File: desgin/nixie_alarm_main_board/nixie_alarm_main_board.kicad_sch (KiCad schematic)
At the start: 1 part, among them U1 ESP32-S3-WROOM-1

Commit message: filter caps
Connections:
- net BUZZER: now also U1.6 (IO6); no longer U1.38 (IO2)
- net DEBUG_UART_RX: now also U1.36 (RXD0); no longer U1.25 (IO48)
- net DEBUG_UART_TX: now also U1.37 (TXD0); no longer U1.24 (IO47)
- net LED_DATA: now also U1.38 (IO2); no longer U1.6 (IO6)
- no-connect marks 11 -> 13

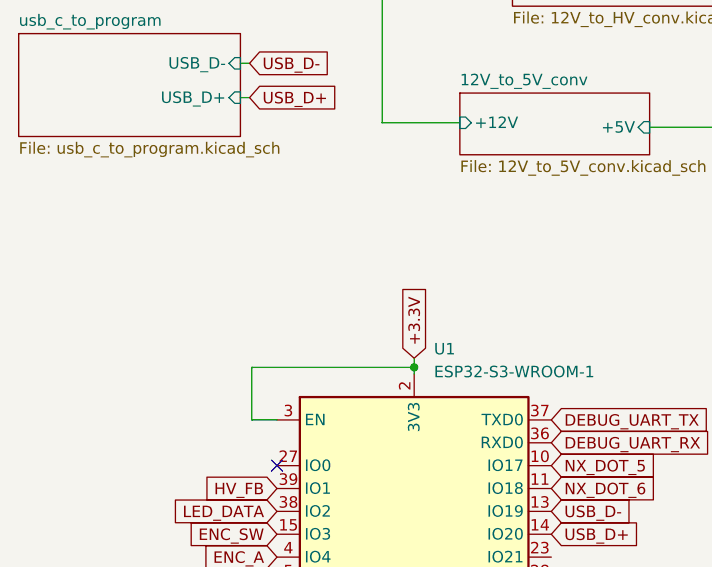
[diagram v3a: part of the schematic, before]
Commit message: all components in board footprint
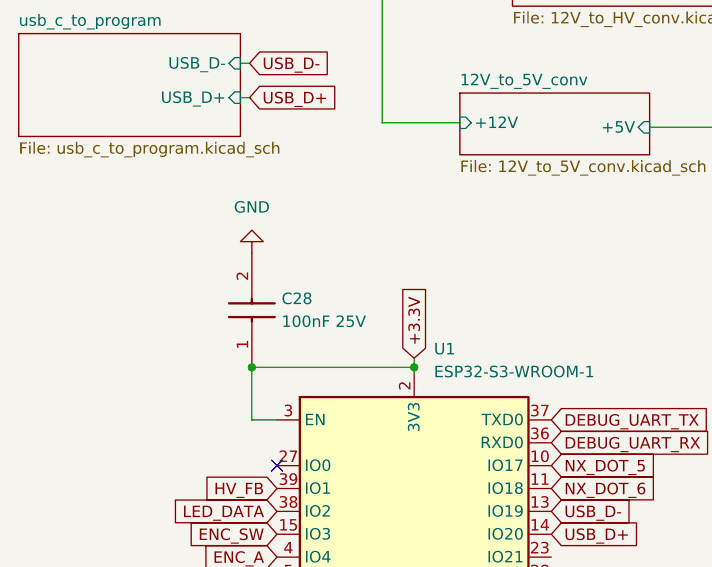
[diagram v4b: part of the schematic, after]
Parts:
- added C28: 100nF 25V, Capacitor_SMD:C_0805_2012Metric_Pad1.18x1.45mm_HandSolder, symbol SamacSys_Parts:GRM033R71E101KA01J
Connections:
- net +3.3V: now also C28.1
- net GND: now also C28.2
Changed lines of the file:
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@@
+		(color 0 0 0 0)
+	)
+	(junction
+		(at 109.474 81.28)
+		(diameter 0)
 		(color 0 0 0 0)
 	)
@@
 	)
 	(symbol
+		(lib_id "SamacSys_Parts:GRM033R71E101KA01J")
+		(at 109.474 81.28 90)
+		(unit 1)
+		(exclude_from_sim no)
+		(in_bom yes)
+		(on_board yes)
+		(dnp no)
+		(fields_autoplaced yes)
+		(property "Reference" "C28"
+			(at 112.776 73.6599 90)
+			(effects
+				(font
+					(size 1.27 1.27)
+				)
+				(justify right)
+			)
+		)
+		(property "Value" "100nF 25V"
+			(at 112.776 76.1999 90)
+			(effects
+				(font
+					(size 1.27 1.27)
+				)
+				(justify right)
+			)
+		)
+		(property "Footprint" "Capacitor_SMD:C_0805_2012Metric_Pad1.18x1.45mm_HandSolder"
+			(at 205.664 72.39 0)
+			(effects
+				(font
+					(size 1.27 1.27)
+				)
+				(justify left top)
+				(hide yes)
+			)
+		)
+		(property "Datasheet" "https://search.murata.co.jp/Ceramy/image/img/A01X/G101/ENG/GRM033R71E101KA01-01A.pdf"
+			(at 305.664 72.39 0)
+			(effects
+				(font
+					(size 1.27 1.27)
+				)
+				(justify left top)
+				(hide yes)
+			)
+		)
+		(property "Description" "Multilayer Ceramic Capacitors MLCC - SMD/SMT 100pF 25 volts 10%"
+			(at 109.474 81.28 0)
+			(effects
+				(font
+					(size 1.27 1.27)
+				)
+				(hide yes)
+			)
+		)
+		(property "Height" "0.5"
+			(at 505.664 72.39 0)
+			(effects
+				(font
+					(size 1.27 1.27)
+				)
+				(justify left top)
+				(hide yes)
+			)
+		)
+		(property "Mouser Part Number" "81-GRM033R71E101KA1J"
+			(at 605.664 72.39 0)
+			(effects
+				(font
+					(size 1.27 1.27)
+				)
+				(justify left top)
+				(hide yes)
+			)
+		)
+		(property "Mouser Price/Stock" "https://www.mouser.co.uk/ProductDetail/Murata-Electronics/GRM033R71E101KA01J?qs=563MOeNa05Lmru4oTW10Jw%3D%3D"
+			(at 705.664 72.39 0)
+			(effects
+				(font
+					(size 1.27 1.27)
+				)
+				(justify left top)
+				(hide yes)
+			)
+		)
+		(property "Manufacturer_Name" "Murata Electronics"
+			(at 805.664 72.39 0)
+			(effects
+				(font
+					(size 1.27 1.27)
+				)
+				(justify left top)
+				(hide yes)
+			)
+		)
+		(property "Manufacturer_Part_Number" "GRM033R71E101KA01J"
+			(at 905.664 72.39 0)
+			(effects
+				(font
+					(size 1.27 1.27)
+				)
+				(justify left top)
+				(hide yes)
+			)
+		)
+		(pin "1"
+		)
+		(pin "2"
+		)
+		(instances
+			(project "nixie_alarm_main_board"
+				(path "/a0d555d7-39a0-4a98-b831-70d97d0aa5a1"
+					(reference "C28")
+					(unit 1)
+				)
+			)
+		)
+	)
+	(symbol
 		(lib_id "power:GND")
 		(at 127.508 137.922 0)
@@
 					(unit 1)
 				)
+			)
+		)
+	)
+	(symbol
+		(lib_id "power:GND")
+		(at 109.474 68.58 180)
+		(unit 1)
+		(exclude_from_sim no)
+		(in_bom yes)
+		(on_board yes)
+		(dnp no)
+		(fields_autoplaced yes)
+		(property "Reference" "#PWR056"
+			(at 109.474 62.23 0)
+			(effects
+				(font
+					(size 1.27 1.27)
+				)
+				(hide yes)
+			)
+		)
+		(property "Value" "GND"
+			(at 109.474 63.5 0)
+			(effects
+				(font
+					(size 1.27 1.27)
+				)
+			)
+		)
+		(property "Footprint" ""
+			(at 109.474 68.58 0)
+			(effects
+				(font
+					(size 1.27 1.27)
+				)
+				(hide yes)
+			)
+		)
+		(property "Datasheet" ""
+			(at 109.474 68.58 0)
+			(effects
+				(font
+					(size 1.27 1.27)
+				)
+				(hide yes)
+			)
+		)
+		(property "Description" "Power symbol creates a global label with name \"GND\" , ground"
+			(at 109.474 68.58 0)
+			(effects
+				(font
+					(size 1.27 1.27)
+				)
+				(hide yes)
+			)
+		)
+		(pin "1"
+		)
+		(instances
+			(project "nixie_alarm_main_board"
+				(path "/a0d555d7-39a0-4a98-b831-70d97d0aa5a1"
+					(reference "#PWR056")
+					(unit 1)
+				)

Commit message: board v1
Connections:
- net BUZZER: now also U1.10 (IO17); no longer U1.6 (IO6)
- net DPOT_SCL: now also U1.24 (IO47); no longer U1.17 (IO9)
- net DPOT_SDA: now also U1.25 (IO48); no longer U1.12 (IO8)
- net ENC_A: now also U1.38 (IO2); no longer U1.4 (IO4)
- net ENC_B: now also U1.31 (IO38); no longer U1.5 (IO5)
- net ENC_SW: now also U1.21 (IO13); no longer U1.15 (IO3)
- net HV_FB: now also U1.11 (IO18); no longer U1.39 (IO1)
- net LED_DATA: now also U1.39 (IO1); no longer U1.38 (IO2)
- net NX_BL: now also U1.15 (IO3); no longer U1.18 (IO10)
- net NX_DATA_INPUT: now also U1.17 (IO9); no longer U1.7 (IO7)
- net NX_DOT_1: now also U1.4 (IO4); no longer U1.21 (IO13)
- net NX_DOT_2: now also U1.9 (IO16); no longer U1.22 (IO14)
- net NX_DOT_3: now also U1.12 (IO8); no longer U1.8 (IO15)
- net NX_DOT_4: now also U1.20 (IO12); no longer U1.9 (IO16)
- net NX_DOT_5: now also U1.22 (IO14); no longer U1.10 (IO17)
- net NX_DOT_6: now also U1.23 (IO21); no longer U1.11 (IO18)
- net NX_LE: now also U1.18 (IO10); no longer U1.20 (IO12)
- no-connect marks 13 -> 10

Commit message: new board v1
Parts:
- removed C28: 100nF 25V, Capacitor_SMD:C_0805_2012Metric_Pad1.18x1.45mm_HandSolder, symbol SamacSys_Parts:GRM033R71E101KA01J
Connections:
- net BUZZER: now also U1.22 (IO14); no longer U1.10 (IO17)
- net ENC_A: now also U1.39 (IO1); no longer U1.38 (IO2)
- net ENC_B: now also U1.38 (IO2); no longer U1.31 (IO38)
- net ENC_SW: now also U1.31 (IO38); no longer U1.21 (IO13)
- net LED_DATA: now also U1.4 (IO4); no longer U1.39 (IO1)
- net NX_BL: now also U1.19 (IO11); no longer U1.15 (IO3)
- net NX_CLK: now also U1.17 (IO9); no longer U1.19 (IO11)
- net NX_DATA_INPUT: now also U1.18 (IO10); no longer U1.17 (IO9)
- net NX_DOT_1: now also U1.5 (IO5); no longer U1.4 (IO4)
- net NX_DOT_2: now also U1.10 (IO17); no longer U1.9 (IO16)
- net NX_DOT_5: now also U1.21 (IO13); no longer U1.22 (IO14)
- net NX_LE: now also U1.15 (IO3); no longer U1.18 (IO10)
- no-connect marks 10 -> 9

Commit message: add more detalis
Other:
- added sheet Debug_UART (Debug_UART.kicad_sch)
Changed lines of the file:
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@@
+	)
+	(sheet
+		(at 82.042 145.796)
+		(size 30.48 12.7)
+		(fields_autoplaced yes)
+		(stroke
+			(width 0.1524)
+			(type solid)
+		)
+		(fill
+			(color 0 0 0 0.0000)
+		)
+		(property "Sheetname" "Debug_UART"
+			(at 82.042 145.0844 0)
+			(effects
+				(font
+					(size 1.27 1.27)
+				)
+				(justify left bottom)
+			)
+		)
+		(property "Sheetfile" "Debug_UART.kicad_sch"
+			(at 82.042 159.0806 0)
+			(effects
+				(font
+					(size 1.27 1.27)
+				)
+				(justify left top)
+			)
+		)
+		(instances
+			(project "nixie_alarm_main_board"
+				(path "/a0d555d7-39a0-4a98-b831-70d97d0aa5a1"
+					(page "11")
+				)
+			)
+		)
 	)
 	(sheet
